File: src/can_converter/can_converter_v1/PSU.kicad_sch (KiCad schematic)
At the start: 6 parts, among them U2 MCP1754ST-3302E/MB

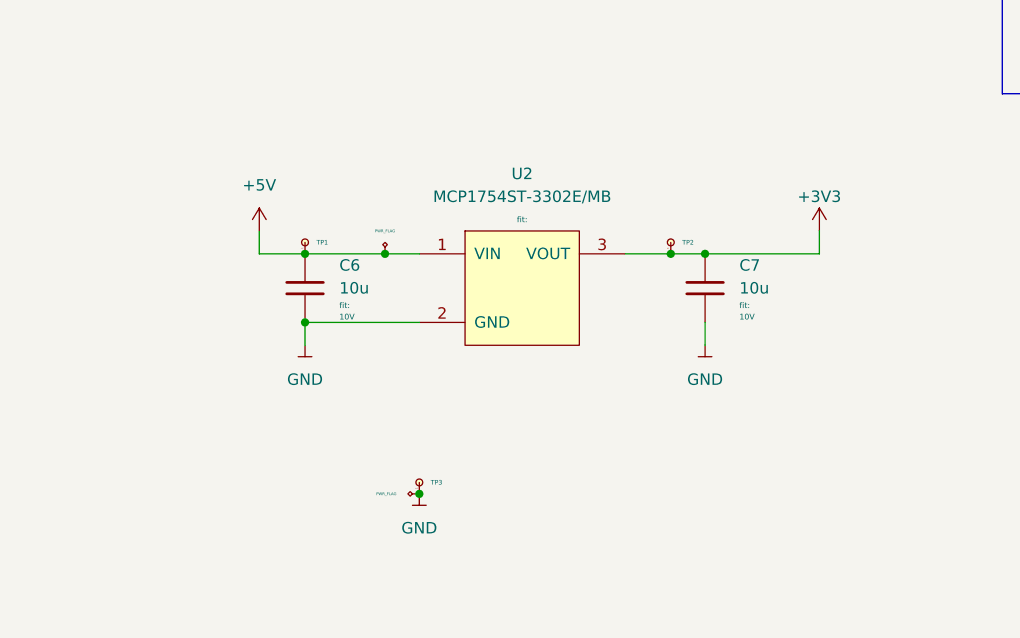
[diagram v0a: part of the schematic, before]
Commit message: Replace regulator and tranceiver
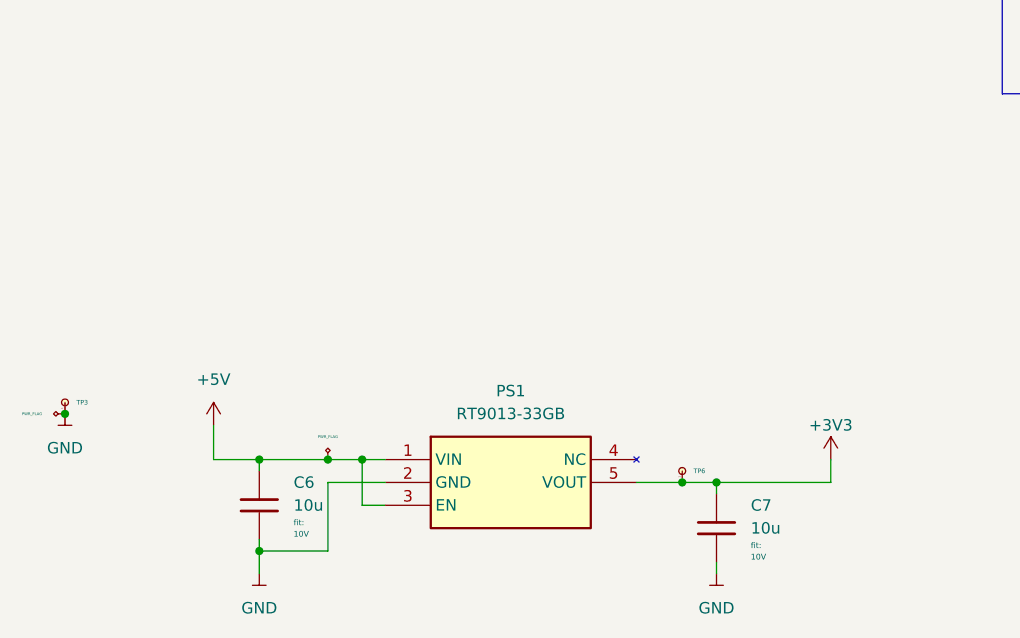
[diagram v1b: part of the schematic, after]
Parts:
- removed TP1, TP2: TP2.0mm, Connector_generic:TP2.0mm, symbol generic-connectors:TP2.0mm
- removed U2: MCP1754ST-3302E/MB, TO_SMD:SOT-89, symbol microchip:MCP1754ST-3302E/MB
- added PS1: RT9013-33GB, SOT94P279X130-5N, symbol RT9013-33GB:RT9013-33GB
- added TP6: TP2.0mm, Connector_generic:TP2.0mm, symbol generic-connectors:TP2.0mm
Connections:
- net +3V3: now also PS1.5 (VOUT), TP6.1
- net +5V: now also PS1.1 (VIN), PS1.3 (EN)
- net GND: now also PS1.2 (GND)
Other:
- moved on the sheet: C6, C7, TP3
